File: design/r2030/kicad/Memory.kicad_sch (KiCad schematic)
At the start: 10 parts, among them U1 SST39SF040, U2 SST39SF040, U3 AS6C4008-55PCN, U4 AS6C4008-55PCN

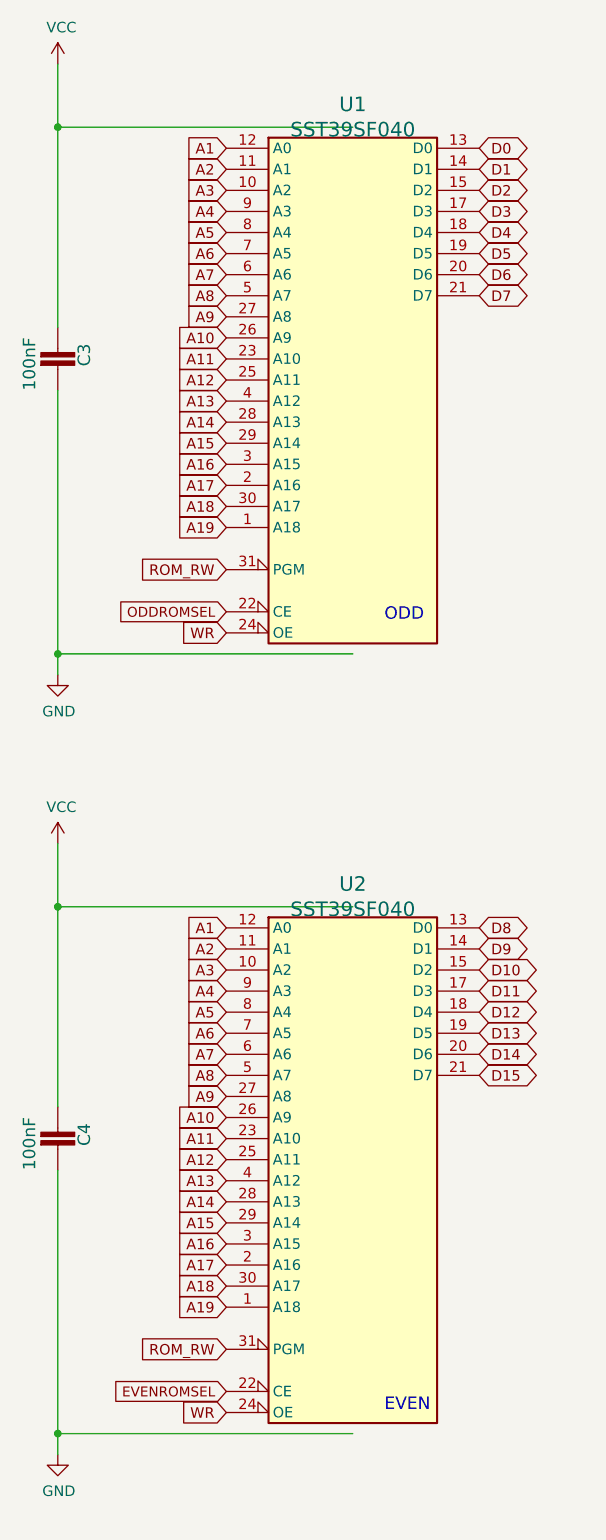
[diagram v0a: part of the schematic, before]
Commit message: Update to Kicad 7
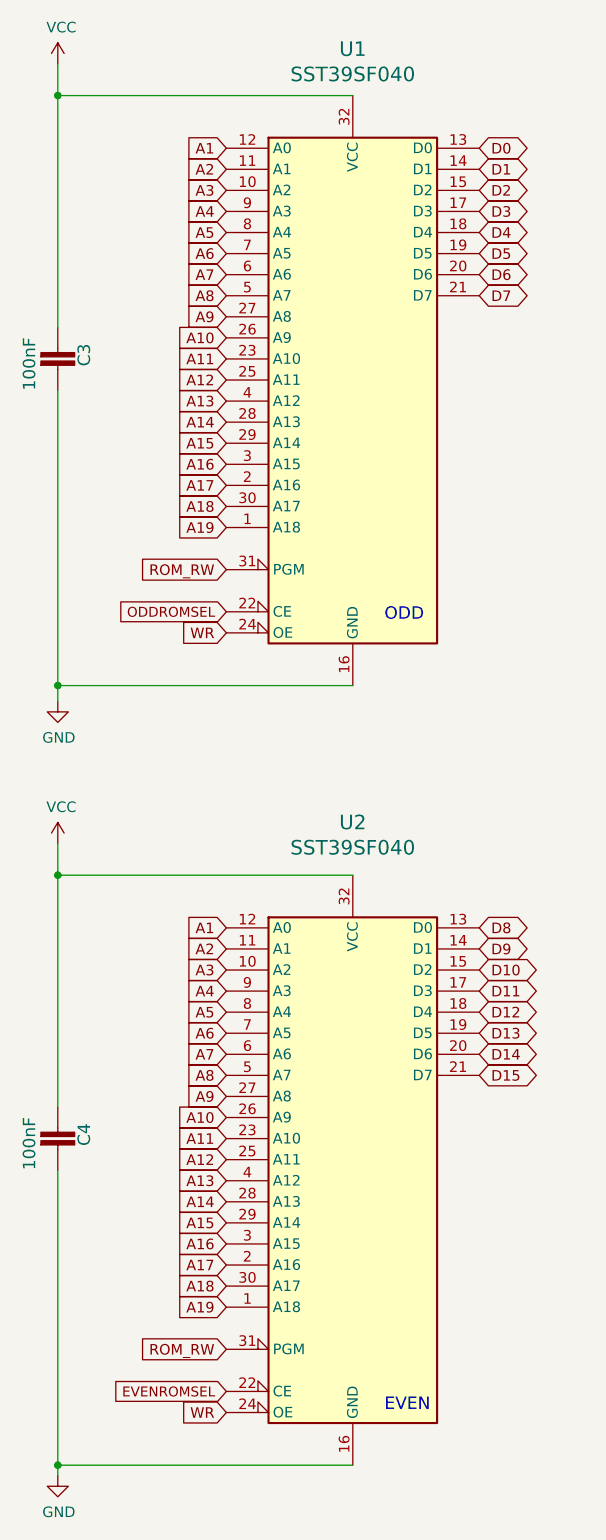
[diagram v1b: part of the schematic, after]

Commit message: Fix pre-prod bugs
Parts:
- U1, U2, U3, U4: footprint Package_DIP:DIP-32_W15.24mm_LongPads -> Package_DIP:DIP-32_W15.24mm_Socket_LongPads
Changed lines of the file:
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@@
   (title_block
     (title "ROSCO_M68K CLASSIC MC68030 EDITION")
-    (date "2023-11-09")
-    (rev "1.0")
+    (date "2023-12-05")
+    (rev "2.0")
     (company "The Really Old-School Company Limited")
     (comment 1 "OSHWA UK000006 (https://certification.oshwa.org/uk000006.html)")
@@
       (effects (font (size 1.7526 1.7526)))
     )
-    (property "Footprint" "Package_DIP:DIP-32_W15.24mm_LongPads" (at 60.96 62.23 0)
+    (property "Footprint" "Package_DIP:DIP-32_W15.24mm_Socket_LongPads" (at 60.96 62.23 0)
       (effects (font (size 1.27 1.27)) hide)
     )
@@
       (effects (font (size 1.7526 1.7526)))
     )
-    (property "Footprint" "Package_DIP:DIP-32_W15.24mm_LongPads" (at 60.96 156.21 0)
+    (property "Footprint" "Package_DIP:DIP-32_W15.24mm_Socket_LongPads" (at 60.96 156.21 0)
       (effects (font (size 1.27 1.27)) hide)
     )
@@
       (effects (font (size 1.7526 1.7526)))
     )
-    (property "Footprint" "Package_DIP:DIP-32_W15.24mm_LongPads" (at 152.4 60.96 0)
+    (property "Footprint" "Package_DIP:DIP-32_W15.24mm_Socket_LongPads" (at 152.4 60.96 0)
       (effects (font (size 1.27 1.27)) hide)
     )
@@
       (effects (font (size 1.7526 1.7526)))
     )
-    (property "Footprint" "Package_DIP:DIP-32_W15.24mm_LongPads" (at 238.76 60.96 0)
-      (effects (font (size 1.27 1.27)) hide)
-    )
+    (property "Footprint" "Package_DIP:DIP-32_W15.24mm_Socket_LongPads" (at 238.76 60.96 0)
+      (effects (font (size 1.27 1.27)) hide)
+    )
